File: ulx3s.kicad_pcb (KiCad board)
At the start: 4 copper layers, 94 x 50.8 mm, 113 parts, among them J1 CONN_02X20, J2 CONN_02X20, J3 WIFI_OFF, Q1 BC857, Q2 2N7002, SW1 DIPSW, U1 LFE5U-25F-6BG381C, U10 S25FL164K0XMFI011, U11 PCA9306DCTR, U2 ESP-32S, U3 AP3429A, U4 AP3429A, U5 AP3429A, U6 FT231XS, U7 PCF8523, U9 MT48LC16M16A2TG, Y1 FNETHE025, Y2 32768Hz

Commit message: top layer GND infill
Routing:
- added copper zone on F.Cu, net GND
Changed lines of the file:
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@@
     (thickness 1.6)
     (drawings 6)
-    (tracks 3933)
+    (tracks 3928)
     (zones 0)
     (modules 145)
@@
   (via (at 134.471354 81.347908) (size 0.4) (drill 0.2) (layers F.Cu B.Cu) (net 123))
   (segment (start 134.344206 75.967565) (end 134.28 75.903359) (width 0.19) (layer In2.Cu) (net 123))
-  (segment (start 114.686808 89.791816) (end 114.914564 89.791816) (width 0.2) (layer In2.Cu) (net 124))
-  (segment (start 114.914564 89.791816) (end 123.977958 80.728422) (width 0.2) (layer In2.Cu) (net 124))
+  (segment (start 97.91 90.63) (end 98.002761 90.722761) (width 0.19) (layer In2.Cu) (net 124))
+  (segment (start 98.002761 90.722761) (end 113.983619 90.722761) (width 0.19) (layer In2.Cu) (net 124))
+  (segment (start 113.983619 90.722761) (end 123.977958 80.728422) (width 0.19) (layer In2.Cu) (net 124))
   (segment (start 132.273875 76.998218) (end 132.47833 77.202673) (width 0.2) (layer In2.Cu) (net 124))
   (segment (start 123.977958 80.728422) (end 124.012976 80.728422) (width 0.2) (layer In2.Cu) (net 124))
@@
   (segment (start 133.403202 78.188707) (end 133.403202 77.806301) (width 0.19) (layer F.Cu) (net 124))
   (segment (start 134.480099 80.600099) (end 134.480099 79.265604) (width 0.19) (layer F.Cu) (net 124))
-  (segment (start 97.91 90.63) (end 98.002761 90.722761) (width 0.19) (layer In2.Cu) (net 124))
-  (segment (start 113.755863 90.722761) (end 114.686808 89.791816) (width 0.19) (layer In2.Cu) (net 124))
-  (segment (start 98.002761 90.722761) (end 113.755863 90.722761) (width 0.19) (layer In2.Cu) (net 124))
-  (segment (start 132.454403 76.676207) (end 132.737245 76.676207) (width 0.19) (layer In2.Cu) (net 125))
-  (segment (start 113.579745 90.40575) (end 122.052891 81.932604) (width 0.19) (layer In2.Cu) (net 125))
-  (segment (start 95.37 90.63) (end 96.455601 89.544399) (width 0.19) (layer In2.Cu) (net 125))
-  (segment (start 127.609799 76.676207) (end 132.454403 76.676207) (width 0.19) (layer In2.Cu) (net 125))
-  (segment (start 122.318384 81.932604) (end 123.844577 80.406411) (width 0.19) (layer In2.Cu) (net 125))
-  (segment (start 123.844577 80.406411) (end 123.879595 80.406411) (width 0.19) (layer In2.Cu) (net 125))
-  (segment (start 99.29244 90.40575) (end 113.579745 90.40575) (width 0.19) (layer In2.Cu) (net 125))
-  (segment (start 98.431089 89.544399) (end 99.29244 90.40575) (width 0.19) (layer In2.Cu) (net 125))
-  (segment (start 96.455601 89.544399) (end 98.431089 89.544399) (width 0.19) (layer In2.Cu) (net 125))
-  (segment (start 123.879595 80.406411) (end 127.609799 76.676207) (width 0.19) (layer In2.Cu) (net 125))
-  (segment (start 122.052891 81.932604) (end 122.318384 81.932604) (width 0.19) (layer In2.Cu) (net 125))
+  (segment (start 132.737245 76.676207) (end 127.609799 76.676207) (width 0.19) (layer In2.Cu) (net 125))
+  (segment (start 127.609799 76.676207) (end 123.879595 80.406411) (width 0.19) (layer In2.Cu) (net 125))
+  (segment (start 99.29244 90.40575) (end 98.431089 89.544399) (width 0.19) (layer In2.Cu) (net 125))
+  (segment (start 123.879595 80.406411) (end 123.844577 80.406411) (width 0.19) (layer In2.Cu) (net 125))
+  (segment (start 123.844577 80.406411) (end 113.845238 90.40575) (width 0.19) (layer In2.Cu) (net 125))
+  (segment (start 113.845238 90.40575) (end 99.29244 90.40575) (width 0.19) (layer In2.Cu) (net 125))
+  (segment (start 98.431089 89.544399) (end 96.455601 89.544399) (width 0.19) (layer In2.Cu) (net 125))
+  (segment (start 96.455601 89.544399) (end 95.37 90.63) (width 0.19) (layer In2.Cu) (net 125))
   (segment (start 134.88 78.1952) (end 133.361007 76.676207) (width 0.19) (layer F.Cu) (net 125))
   (segment (start 134.88 80.2) (end 134.88 78.1952) (width 0.19) (layer F.Cu) (net 125))
@@
       )
     )
+  )
+  (zone (net 1) (net_name GND) (layer F.Cu) (hatch edge 0.508)
+    (connect_pads (clearance 0.254))
+    (min_thickness 0.254)
+    (fill yes (arc_segments 16) (thermal_gap 0.508) (thermal_bridge_width 0.508))
+    (polygon
+      (pts
+        (xy 94.1 112.22) (xy 188.08 112.22) (xy 188.08 61.42) (xy 94.1 61.42)
+      )
+    )

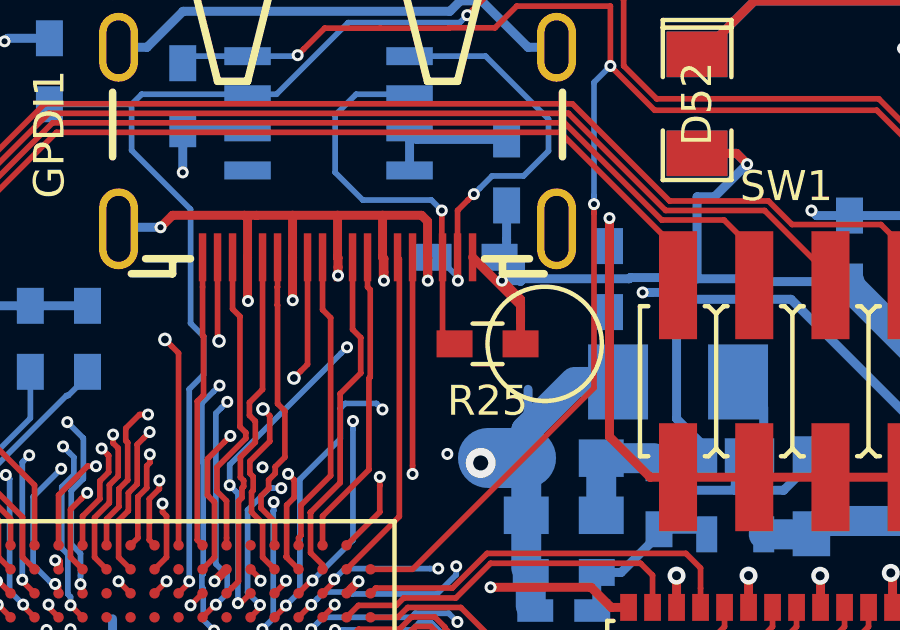
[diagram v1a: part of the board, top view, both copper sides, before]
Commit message: R25 moved away from OLED screw hole (to the bottom side)
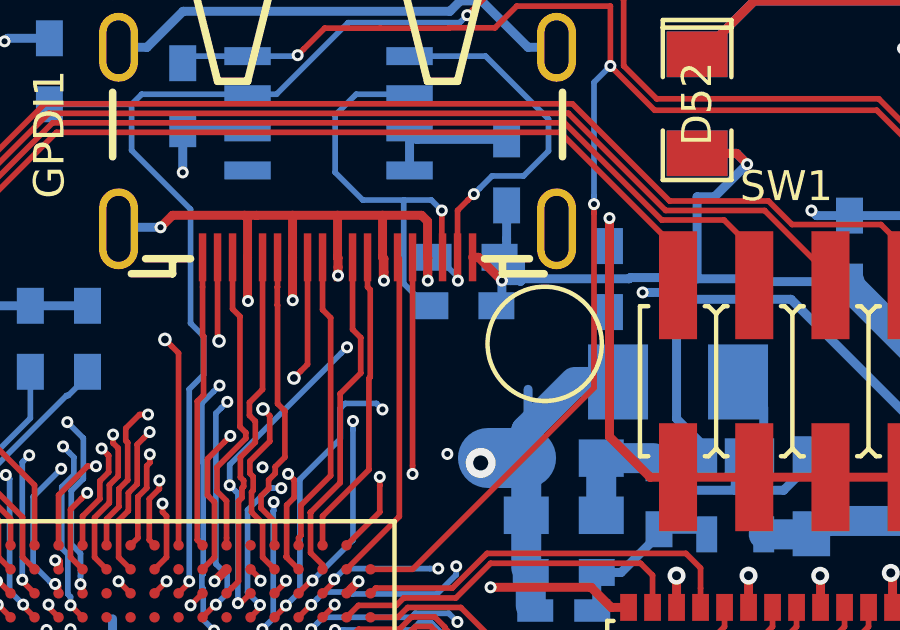
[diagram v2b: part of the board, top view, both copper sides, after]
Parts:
- R25: moved to B.Cu
- moved R25 1.50 mm to (149.2, 72.2)
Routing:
- net +5V: track 206.1 -> 203.1 mm
- net GPDI_5V_SCL: track 13.4 -> 14.6 mm
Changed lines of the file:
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@@
     (thickness 1.6)
     (drawings 6)
-    (tracks 3928)
+    (tracks 3929)
     (zones 0)
     (modules 145)
@@
     )
   )
-  (module Resistors_SMD:R_0603_HandSoldering (layer F.Cu)
-    (at 149.98 73.485 180)
+  (module Resistors_SMD:R_0603_HandSoldering (layer B.Cu)
+    (at 149.175 72.215 180)
     (descr "Resistor SMD 0603, hand soldering")
     (tags "resistor 0603")
     (attr smd)
-    (fp_text reference R25 (at 0 -1.9 180) (layer F.SilkS)
-      (effects (font (size 1 1) (thickness 0.15)))
+    (fp_text reference R25 (at 0 1.9 180) (layer B.SilkS)
+      (effects (font (size 1 1) (thickness 0.15)) (justify mirror))
     )
-    (fp_text value 470 (at 0 1.9 180) (layer F.Fab)
-      (effects (font (size 1 1) (thickness 0.15)))
+    (fp_text value 470 (at 0 -1.9 180) (layer B.Fab)
+      (effects (font (size 1 1) (thickness 0.15)) (justify mirror))
     )
-    (fp_line (start -0.8 0.4) (end -0.8 -0.4) (layer F.Fab) (width 0.1))
-    (fp_line (start 0.8 0.4) (end -0.8 0.4) (layer F.Fab) (width 0.1))
-    (fp_line (start 0.8 -0.4) (end 0.8 0.4) (layer F.Fab) (width 0.1))
-    (fp_line (start -0.8 -0.4) (end 0.8 -0.4) (layer F.Fab) (width 0.1))
-    (fp_line (start -2 -0.8) (end 2 -0.8) (layer F.CrtYd) (width 0.05))
-    (fp_line (start -2 0.8) (end 2 0.8) (layer F.CrtYd) (width 0.05))
-    (fp_line (start -2 -0.8) (end -2 0.8) (layer F.CrtYd) (width 0.05))
-    (fp_line (start 2 -0.8) (end 2 0.8) (layer F.CrtYd) (width 0.05))
-    (fp_line (start 0.5 0.675) (end -0.5 0.675) (layer F.SilkS) (width 0.15))
-    (fp_line (start -0.5 -0.675) (end 0.5 -0.675) (layer F.SilkS) (width 0.15))
-    (pad 1 smd rect (at -1.1 0 180) (size 1.2 0.9) (layers F.Cu F.Paste F.Mask)
+    (fp_line (start -0.8 -0.4) (end -0.8 0.4) (layer B.Fab) (width 0.1))
+    (fp_line (start 0.8 -0.4) (end -0.8 -0.4) (layer B.Fab) (width 0.1))
+    (fp_line (start 0.8 0.4) (end 0.8 -0.4) (layer B.Fab) (width 0.1))
+    (fp_line (start -0.8 0.4) (end 0.8 0.4) (layer B.Fab) (width 0.1))
+    (fp_line (start -2 0.8) (end 2 0.8) (layer B.CrtYd) (width 0.05))
+    (fp_line (start -2 -0.8) (end 2 -0.8) (layer B.CrtYd) (width 0.05))
+    (fp_line (start -2 0.8) (end -2 -0.8) (layer B.CrtYd) (width 0.05))
+    (fp_line (start 2 0.8) (end 2 -0.8) (layer B.CrtYd) (width 0.05))
+    (fp_line (start 0.5 -0.675) (end -0.5 -0.675) (layer B.SilkS) (width 0.15))
+    (fp_line (start -0.5 0.675) (end 0.5 0.675) (layer B.SilkS) (width 0.15))
+    (pad 1 smd rect (at -1.1 0 180) (size 1.2 0.9) (layers B.Cu B.Paste B.Mask)
       (net 2 +5V))
-    (pad 2 smd rect (at 1.1 0 180) (size 1.2 0.9) (layers F.Cu F.Paste F.Mask)
+    (pad 2 smd rect (at 1.1 0 180) (size 1.2 0.9) (layers B.Cu B.Paste B.Mask)
       (net 39 GPDI_5V_SCL))
     (model Resistors_SMD.3dshapes/R_0603_HandSoldering.wrl
@@
   (segment (start 142.88 94.6) (end 142.88 93.8) (width 0.3) (layer F.Cu) (net 1))
   (segment (start 145.28 93.8) (end 145.28 94.6) (width 0.3) (layer F.Cu) (net 1))
+  (segment (start 150.457224 71.377791) (end 150.457224 72.032776) (width 0.3) (layer B.Cu) (net 2))
+  (segment (start 150.457224 72.032776) (end 150.275 72.215) (width 0.3) (layer B.Cu) (net 2))
+  (segment (start 149.48 70.6) (end 149.679433 70.6) (width 0.3) (layer F.Cu) (net 2))
+  (segment (start 149.679433 70.6) (end 150.457224 71.377791) (width 0.3) (layer F.Cu) (net 2))
   (segment (start 107.307001 96.98944) (end 102.731849 92.414288) (width 1) (layer In1.Cu) (net 2))
   (segment (start 134.105 111.136459) (end 119.803256 111.136459) (width 1) (layer In1.Cu) (net 2))
@@
   (via (at 150.457224 71.377791) (size 0.4) (drill 0.2) (layers F.Cu B.Cu) (net 2))
   (segment (start 151.057791 71.377791) (end 150.740066 71.377791) (width 0.3) (layer B.Cu) (net 2))
-  (segment (start 151.08 72.000567) (end 150.657223 71.57779) (width 0.3) (layer F.Cu) (net 2))
   (segment (start 150.740066 71.377791) (end 150.457224 71.377791) (width 0.3) (layer B.Cu) (net 2))
   (segment (start 151.08 71.4) (end 151.057791 71.377791) (width 0.3) (layer B.Cu) (net 2))
-  (segment (start 151.08 72.735) (end 151.08 72.000567) (width 0.3) (layer F.Cu) (net 2))
-  (segment (start 150.657223 71.57779) (end 150.457224 71.377791) (width 0.3) (layer F.Cu) (net 2))
   (segment (start 166.28 97.918756) (end 166.233987 97.964769) (width 1) (layer In2.Cu) (net 2))
   (segment (start 134.105 111.136459) (end 134.412661 111.44412) (width 1) (layer In1.Cu) (net 2))
@@
   (segment (start 101.085 83.665) (end 102.553083 83.665) (width 0.3) (layer B.Cu) (net 2))
   (via (at 102.731849 83.486234) (size 1) (drill 0.5) (layers F.Cu B.Cu) (net 2))
-  (segment (start 151.08 73.485) (end 151.08 72.735) (width 0.3) (layer F.Cu) (net 2))
-  (segment (start 151.08 72.2) (end 151.08 72.735) (width 0.3) (layer F.Cu) (net 2))
-  (segment (start 149.48 70.6) (end 151.08 72.2) (width 0.3) (layer F.Cu) (net 2))
   (segment (start 106.419 69.675) (end 106.419 69.929) (width 0.3) (layer B.Cu) (net 2))
   (segment (start 100.572432 83.665) (end 100.424079 83.813353) (width 0.3) (layer B.Cu) (net 2))
@@
   (segment (start 132.835 72.217) (end 134.74 72.217) (width 0.3) (layer B.Cu) (net 38))
   (segment (start 130.93 72.217) (end 132.835 72.217) (width 0.3) (layer B.Cu) (net 38))
+  (segment (start 145.821785 68.691785) (end 147.186 68.691785) (width 0.19) (layer B.Cu) (net 39))
+  (segment (start 147.186 68.691785) (end 148.107785 68.691785) (width 0.19) (layer B.Cu) (net 39))
+  (segment (start 148.075 72.215) (end 147.925 72.215) (width 0.19) (layer B.Cu) (net 39))
+  (segment (start 147.186 71.476) (end 147.186 68.691785) (width 0.19) (layer B.Cu) (net 39))
+  (segment (start 147.925 72.215) (end 147.186 71.476) (width 0.19) (layer B.Cu) (net 39))
+  (segment (start 148.075 72.215) (end 148.075 71.961) (width 0.19) (layer B.Cu) (net 39))
   (segment (start 147.38 65.165) (end 145.6 65.165) (width 0.19) (layer B.Cu) (net 39))
   (segment (start 145.6 65.165) (end 144.9 65.865) (width 0.19) (layer B.Cu) (net 39))
   (segment (start 144.9 65.865) (end 144.9 67.77) (width 0.19) (layer B.Cu) (net 39))
   (segment (start 144.9 67.77) (end 145.821785 68.691785) (width 0.19) (layer B.Cu) (net 39))
-  (segment (start 145.821785 68.691785) (end 148.107785 68.691785) (width 0.19) (layer B.Cu) (net 39))
   (segment (start 148.107785 68.691785) (end 148.456 69.04) (width 0.19) (layer B.Cu) (net 39))
   (segment (start 148.456 69.04) (end 148.456 70.576) (width 0.19) (layer F.Cu) (net 39))
   (segment (start 148.456 70.576) (end 148.48 70.6) (width 0.19) (layer F.Cu) (net 39))
   (via (at 148.456 69.04) (size 0.4) (drill 0.2) (layers F.Cu B.Cu) (net 39))
-  (segment (start 148.48 70.6) (end 148.48 73.085) (width 0.19) (layer F.Cu) (net 39))
-  (segment (start 148.48 73.085) (end 148.88 73.485) (width 0.19) (layer F.Cu) (net 39))
   (segment (start 148.98 69.038979) (end 149.324337 68.694642) (width 0.19) (layer F.Cu) (net 40))
   (segment (start 148.98 70.6) (end 148.98 69.038979) (width 0.19) (layer F.Cu) (net 40))

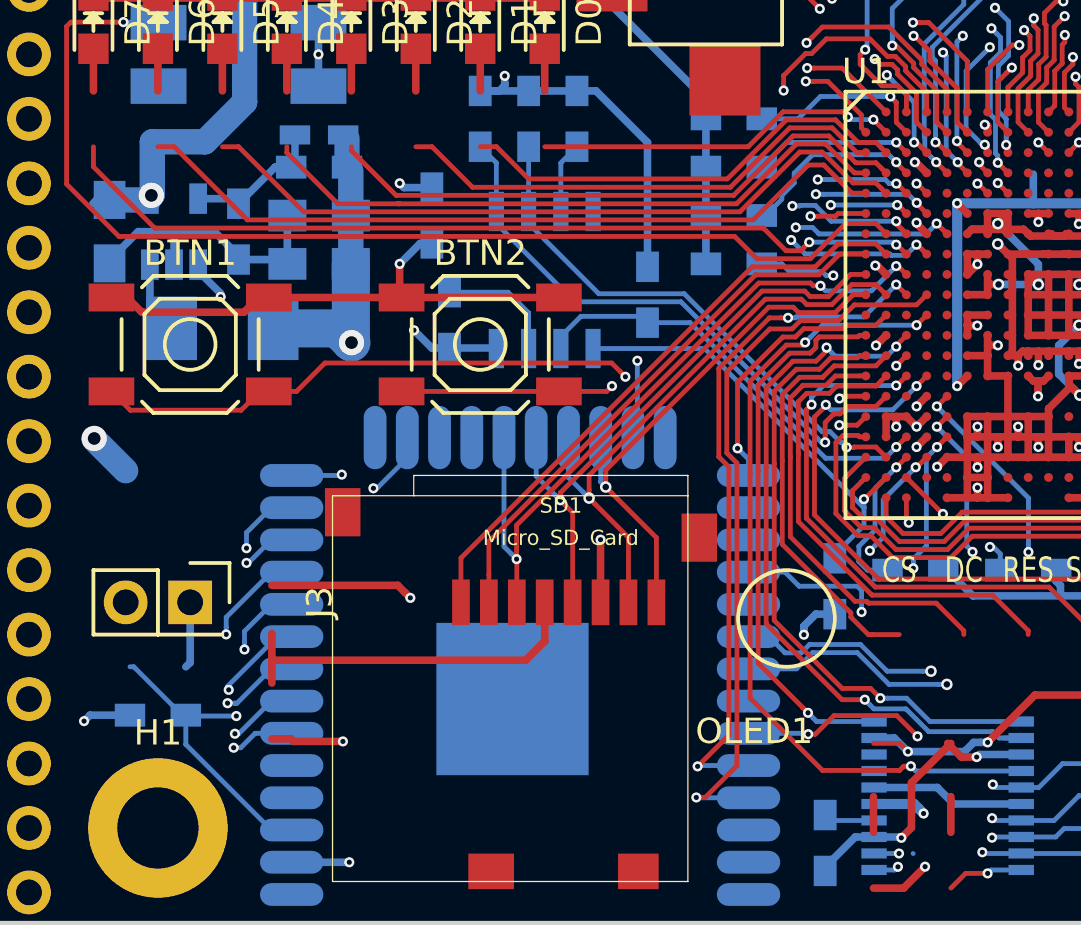
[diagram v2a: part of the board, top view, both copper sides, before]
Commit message: connecting almost all free pins from ESP32 to FPGA (only 4 left unconnected)
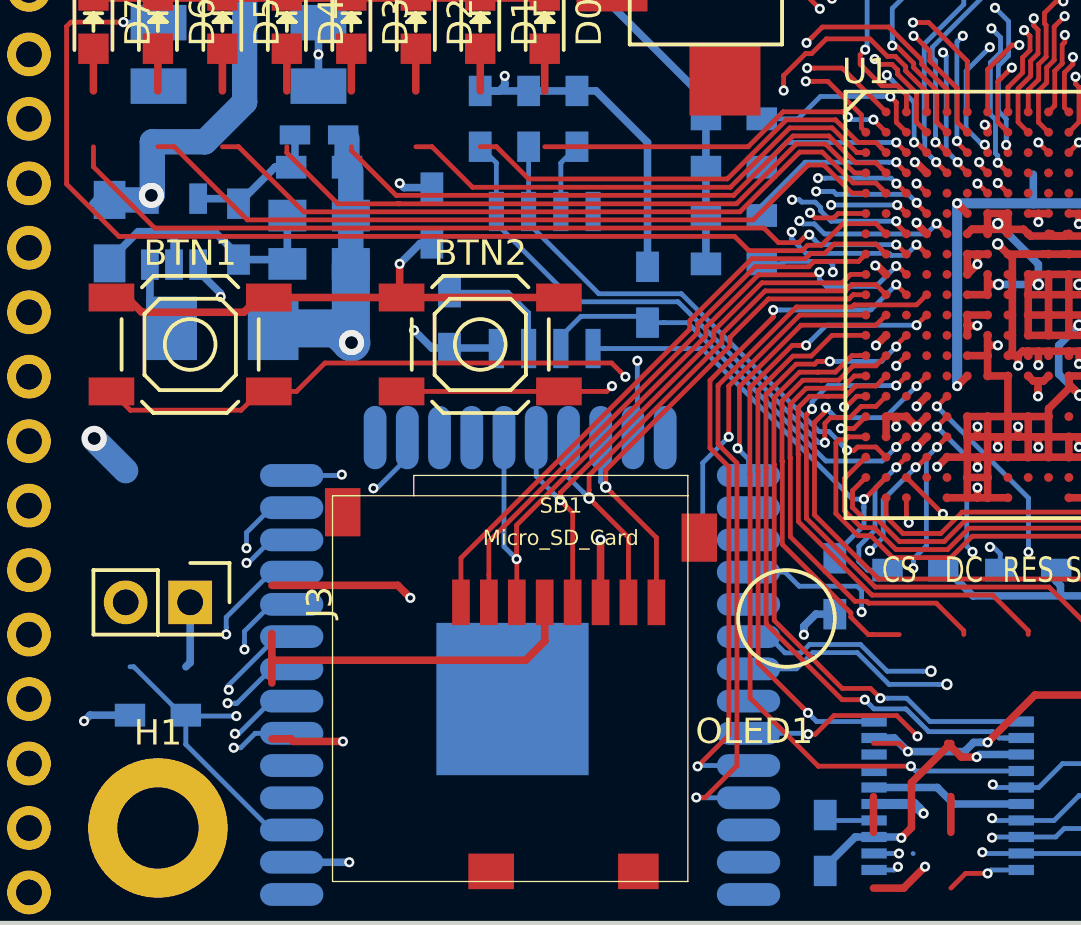
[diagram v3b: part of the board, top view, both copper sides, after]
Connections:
- net WIFI_15 renamed WIFI_GPIO15
- U1 pad L1: (no net) -> WIFI_GPIO16
- U2 pad 27: (no net) -> WIFI_GPIO16
- U2 pad 38: (no net) -> GND
- U2 pad 39: (no net) -> GND
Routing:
- net WIFI_GPIO16: track 0.00 -> 14.6 mm, vias 0 -> 1
- net SD_CMD: track 28.0 -> 28.6 mm

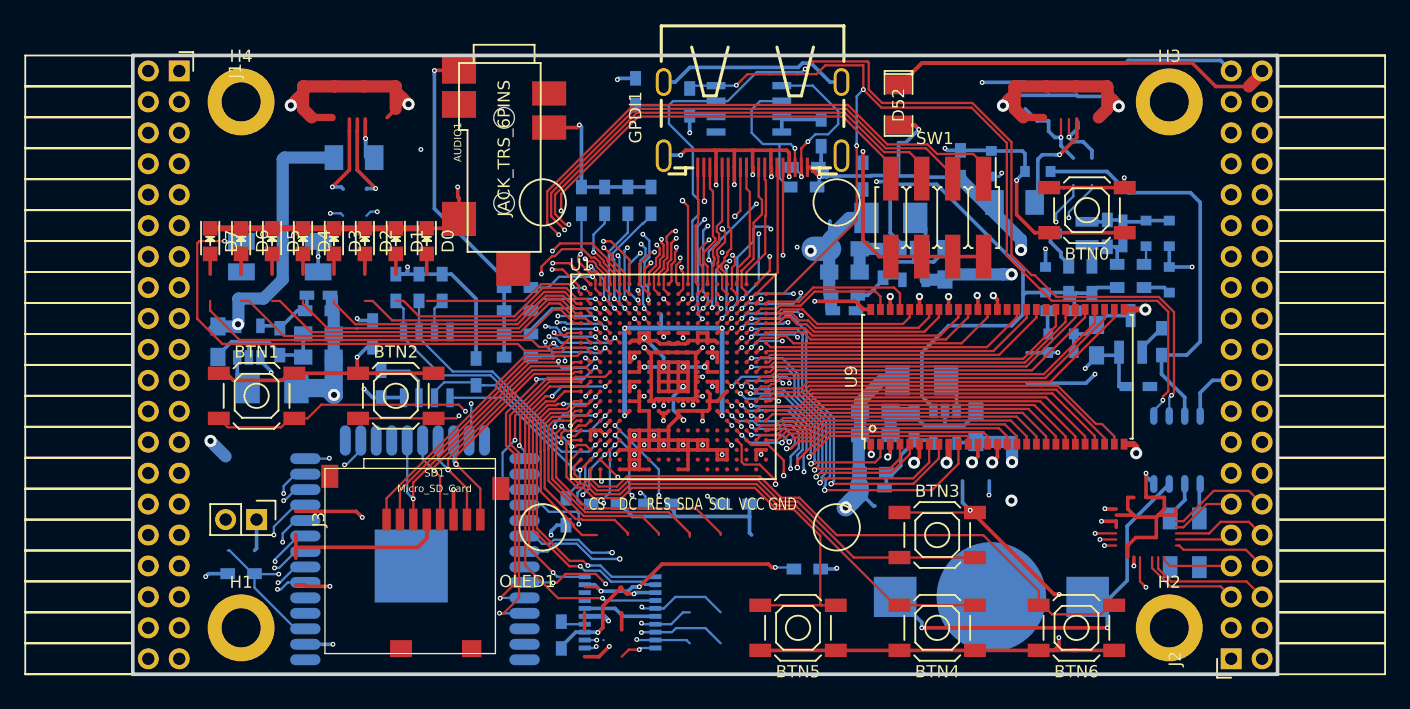
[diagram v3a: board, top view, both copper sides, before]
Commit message: small changes, moving the traces
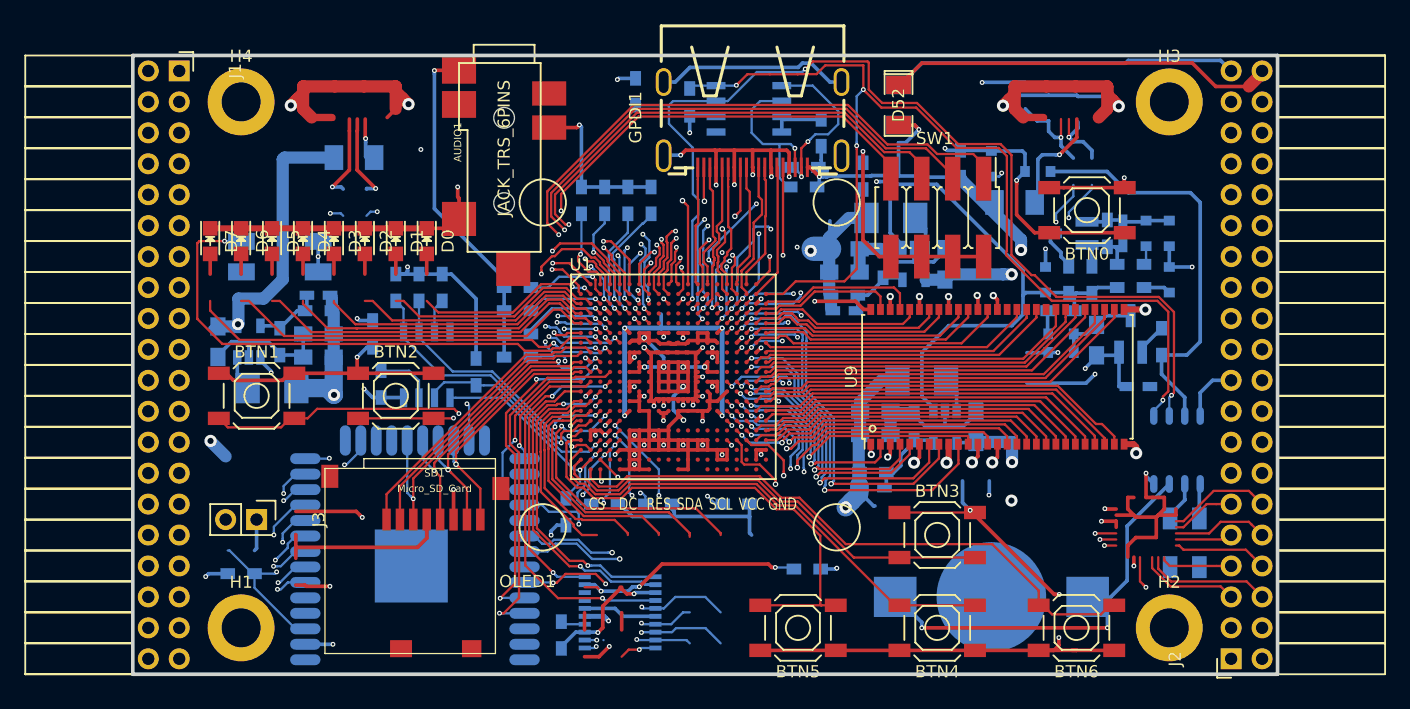
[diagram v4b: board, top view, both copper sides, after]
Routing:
- net GPDI_SDA: track 85.1 -> 86.8 mm
- net LED0: track 14.4 -> 15.1 mm
- net GPDI_SCL: track 87.3 -> 86.6 mm
